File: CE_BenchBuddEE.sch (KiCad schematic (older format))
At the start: 0 parts

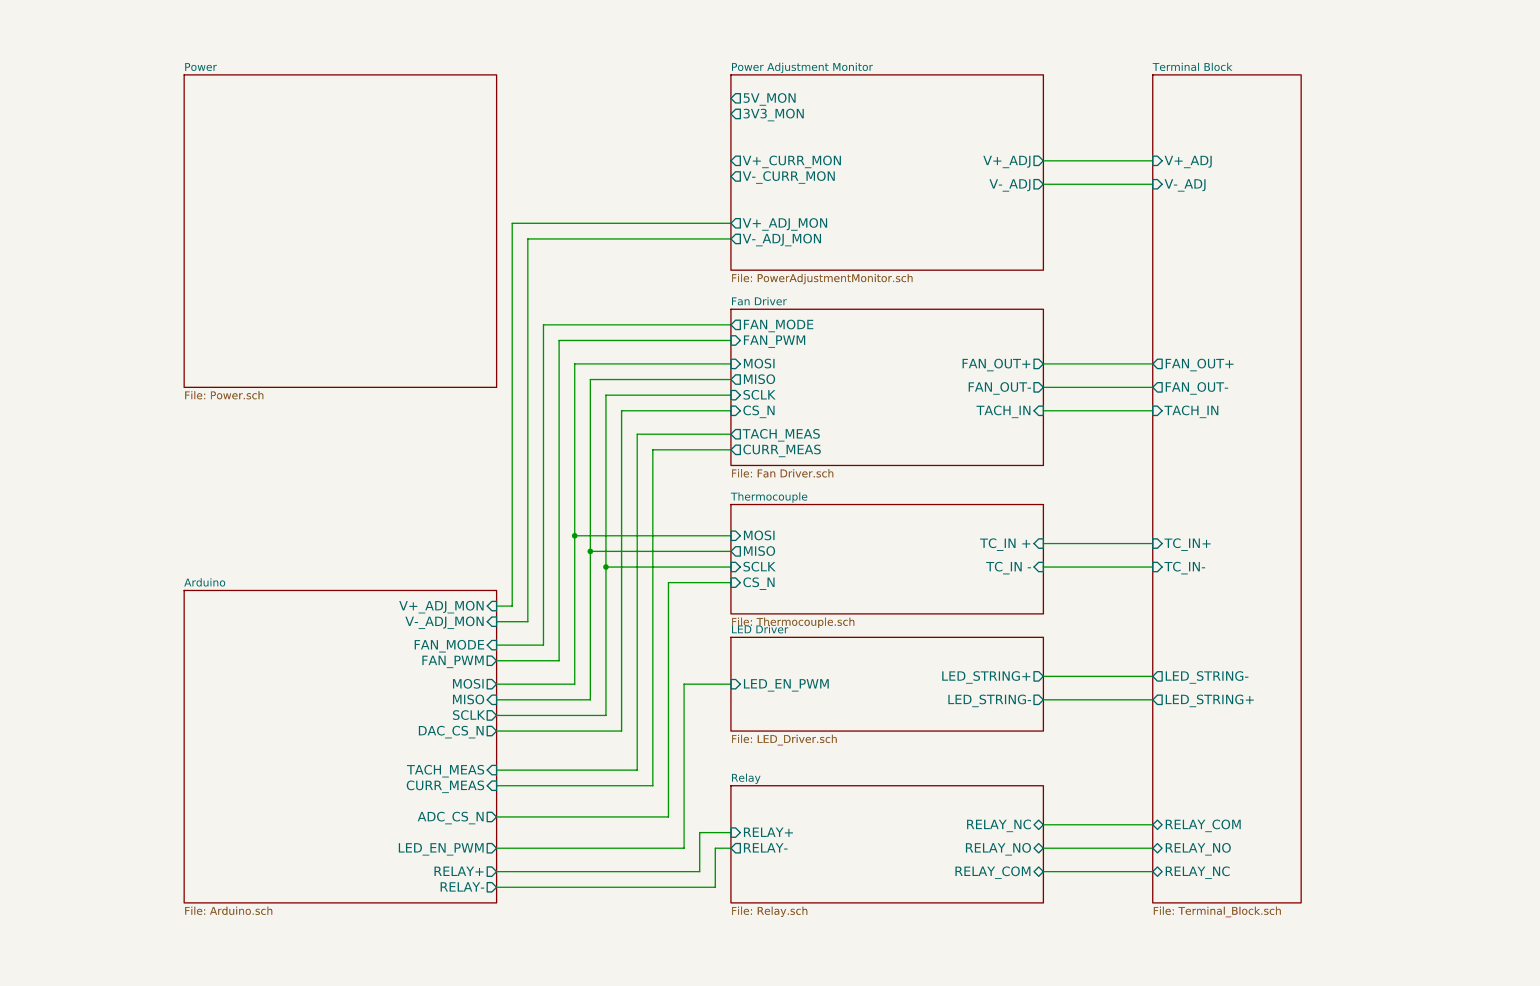
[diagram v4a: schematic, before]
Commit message: Initial layout of relay and thermocouple
All block diagrams completed through Week 3.  Component selection
spreadsheets created: Bench Buddy Session 1CE.xlsx = official part
selection and bom.xlsx is the version I came up with.

Part association and initial layout of the Relay and Thermocouple
sections completed.
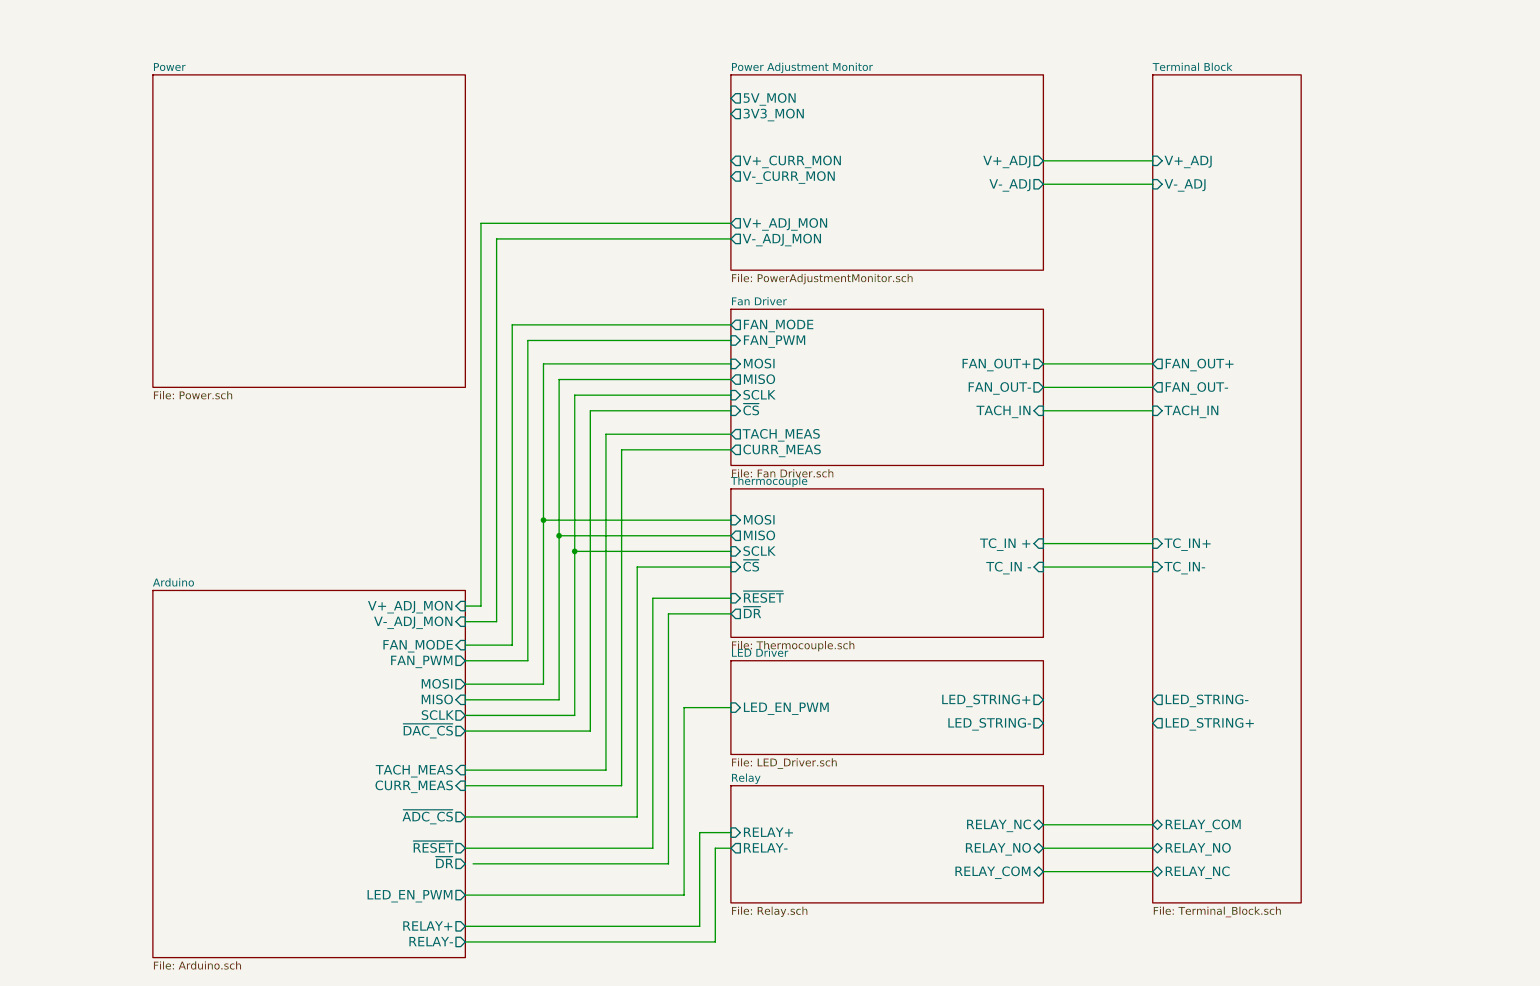
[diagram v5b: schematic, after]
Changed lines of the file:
@@
 Sheet 1 9
 Title ""
-Date "6 feb 2014"
+Date "21 feb 2014"
 Rev ""
 Comp ""
@@
 $EndDescr
 $Sheet
-S 5400 4150 2000 700
+S 5400 4050 2000 950
 U 52EBF2F6
 F0 "Thermocouple" 50
 F1 "Thermocouple.sch" 50
-F2 "MOSI" I L 5400 4350 60
-F3 "MISO" O L 5400 4450 60
-F4 "SCLK" I L 5400 4550 60
-F5 "CS_N" I L 5400 4650 60
-F6 "TC_IN +" I R 7400 4400 60
-F7 "TC_IN -" I R 7400 4550 60
+F2 "MOSI" I L 5400 4250 60
+F3 "MISO" O L 5400 4350 60
+F4 "SCLK" I L 5400 4450 60
+F5 "TC_IN +" I R 7400 4400 60
+F6 "TC_IN -" I R 7400 4550 60
+F7 "~CS" I L 5400 4550 60
+F8 "~RESET" I L 5400 4750 60
+F9 "~DR" O L 5400 4850 60
 $EndSheet
 $Sheet
@@
 $EndSheet
 $Sheet
-S 1900 1400 2000 2000
+S 1700 1400 2000 2000
 U 52EBF30F
 F0 "Power" 50
@@
 $EndSheet
 $Sheet
-S 5400 5000 2000 600
+S 5400 5150 2000 600
 U 52EBF33E
 F0 "LED Driver" 50
 F1 "LED_Driver.sch" 50
-F2 "LED_EN_PWM" I L 5400 5300 60
-F3 "LED_STRING+" O R 7400 5250 60
-F4 "LED_STRING-" O R 7400 5400 60
+F2 "LED_EN_PWM" I L 5400 5450 60
+F3 "LED_STRING+" O R 7400 5400 60
+F4 "LED_STRING-" O R 7400 5550 60
 $EndSheet
 $Sheet
@@
 F2 "MOSI" I L 5400 3250 60
 F3 "MISO" O L 5400 3350 60
-F4 "CS_N" I L 5400 3550 60
+F4 "~CS" I L 5400 3550 60
 F5 "SCLK" I L 5400 3450 60
 F6 "FAN_OUT+" O R 7400 3250 60
@@
 F5 "FAN_OUT-" O L 8100 3400 60
 F6 "TACH_IN" I L 8100 3550 60
-F7 "LED_STRING+" O L 8100 5400 60
-F8 "LED_STRING-" O L 8100 5250 60
+F7 "LED_STRING+" O L 8100 5550 60
+F8 "LED_STRING-" O L 8100 5400 60
 F9 "TC_IN+" I L 8100 4400 60
 F10 "TC_IN-" I L 8100 4550 60
@@
 F13 "RELAY_NC" B L 8100 6500 60
 $EndSheet
-$Sheet
-S 1900 4700 2000 2000
+Wire Wire Line
+	8100 1950 7400 1950
+Wire Wire Line
+	8100 2100 7400 2100
+Wire Wire Line
+	7400 3250 8100 3250
+Wire Wire Line
+	7400 3400 8100 3400
+Wire Wire Line
+	8100 3550 7400 3550
+Wire Wire Line
+	7400 4400 8100 4400
+Wire Wire Line
+	8100 4550 7400 4550
+Wire Wire Line
+	7400 6200 8100 6200
+Wire Wire Line
+	7400 6350 8100 6350
+Wire Wire Line
+	7400 6500 8100 6500
+Wire Wire Line
+	3700 4800 3800 4800
+Wire Wire Line
+	3800 4800 3800 2350
+Wire Wire Line
+	3800 2350 5400 2350
+Wire Wire Line
+	5400 2450 3900 2450
+Wire Wire Line
+	3900 2450 3900 4900
+Wire Wire Line
+	3900 4900 3700 4900
+Wire Wire Line
+	5400 3700 4600 3700
+Wire Wire Line
+	5400 3800 4700 3800
+Wire Wire Line
+	3700 5850 4600 5850
+Wire Wire Line
+	4600 5850 4600 3700
+Wire Wire Line
+	4700 3800 4700 5950
+Wire Wire Line
+	4700 5950 3700 5950
+Wire Wire Line
+	4800 6150 3700 6150
+Wire Wire Line
+	4800 4550 4800 6150
+Wire Wire Line
+	5100 5450 5100 6650
+Wire Wire Line
+	5100 5450 5400 5450
+Wire Wire Line
+	5200 6250 5200 6850
+Wire Wire Line
+	5200 6250 5400 6250
+Wire Wire Line
+	5400 6350 5300 6350
+Wire Wire Line
+	5300 6350 5300 6950
+Wire Wire Line
+	4200 5300 3700 5300
+Wire Wire Line
+	4300 5400 3700 5400
+Wire Wire Line
+	4400 5500 3700 5500
+Wire Wire Line
+	3700 5600 4500 5600
+Wire Wire Line
+	5400 3100 4100 3100
+Wire Wire Line
+	4100 3100 4100 5150
+Wire Wire Line
+	4100 5150 3700 5150
+Wire Wire Line
+	3700 5050 4000 5050
+Wire Wire Line
+	4000 5050 4000 3000
+Wire Wire Line
+	4000 3000 5400 3000
+Wire Wire Line
+	4500 3550 5400 3550
+Wire Wire Line
+	4400 3450 5400 3450
+Wire Wire Line
+	4300 3350 5400 3350
+Wire Wire Line
+	4200 3250 5400 3250
+Wire Wire Line
+	4200 3250 4200 5300
+Wire Wire Line
+	4300 3350 4300 5400
+Wire Wire Line
+	4400 3450 4400 5500
+Wire Wire Line
+	4500 5600 4500 3550
+$Sheet
+S 1700 4700 2000 2350
 U 52EBF29E
 F0 "Arduino" 50
 F1 "Arduino.sch" 50
-F2 "MOSI" O R 3900 5300 60
-F3 "MISO" I R 3900 5400 60
-F4 "SCLK" O R 3900 5500 60
-F5 "TACH_MEAS" I R 3900 5850 60
-F6 "LED_EN_PWM" O R 3900 6350 60
-F7 "CURR_MEAS" I R 3900 5950 60
-F8 "RELAY+" O R 3900 6500 60
-F9 "RELAY-" O R 3900 6600 60
-F10 "V+_ADJ_MON" I R 3900 4800 60
-F11 "V-_ADJ_MON" I R 3900 4900 60
-F12 "DAC_CS_N" O R 3900 5600 60
-F13 "ADC_CS_N" O R 3900 6150 60
-F14 "FAN_PWM" O R 3900 5150 60
-F15 "FAN_MODE" I R 3900 5050 60
-$EndSheet
-Wire Wire Line
-	8100 1950 7400 1950
-Wire Wire Line
-	8100 2100 7400 2100
-Wire Wire Line
-	7400 3250 8100 3250
-Wire Wire Line
-	7400 3400 8100 3400
-Wire Wire Line
-	8100 3550 7400 3550
-Wire Wire Line
-	7400 4400 8100 4400
-Wire Wire Line
-	8100 4550 7400 4550
-Wire Wire Line
-	7400 5250 8100 5250
-Wire Wire Line
-	7400 5400 8100 5400
-Wire Wire Line
-	7400 6200 8100 6200
-Wire Wire Line
-	7400 6350 8100 6350
-Wire Wire Line
-	7400 6500 8100 6500
-Wire Wire Line
-	3900 4800 4000 4800
-Wire Wire Line
-	4000 4800 4000 2350
-Wire Wire Line
-	4000 2350 5400 2350
-Wire Wire Line
-	5400 2450 4100 2450
-Wire Wire Line
-	4100 2450 4100 4900
-Wire Wire Line
-	4100 4900 3900 4900
-Wire Wire Line
-	5400 3700 4800 3700
-Wire Wire Line
-	5400 3800 4900 3800
-Wire Wire Line
-	3900 5850 4800 5850
-Wire Wire Line
-	4800 5850 4800 3700
-Wire Wire Line
-	4900 3800 4900 5950
-Wire Wire Line
-	4900 5950 3900 5950
-Wire Wire Line
-	3900 6150 5000 6150
-Wire Wire Line
-	5000 6150 5000 4650
-Wire Wire Line
-	5000 4650 5400 4650
-Wire Wire Line
-	3900 6350 5100 6350
-Wire Wire Line
-	5100 6350 5100 5300
-Wire Wire Line
-	5100 5300 5400 5300
-Wire Wire Line
-	3900 6500 5200 6500
-Wire Wire Line
-	5200 6500 5200 6250
-Wire Wire Line
-	5200 6250 5400 6250
-Wire Wire Line
-	5400 6350 5300 6350
-Wire Wire Line
-	5300 6350 5300 6600
-Wire Wire Line
-	5300 6600 3900 6600
-Wire Wire Line
-	4400 5300 3900 5300
-Wire Wire Line
-	4500 5400 3900 5400
-Wire Wire Line
-	4600 5500 3900 5500
-Wire Wire Line
-	5400 4350 4400 4350
-Connection ~ 4400 4350
-Wire Wire Line
-	5400 4450 4500 4450
-Connection ~ 4500 4450
-Wire Wire Line
-	5400 4550 4600 4550
-Connection ~ 4600 4550
-Wire Wire Line
-	3900 5600 4700 5600
-Wire Wire Line
-	5400 3100 4300 3100
-Wire Wire Line
-	4300 3100 4300 5150
-Wire Wire Line
-	4300 5150 3900 5150
-Wire Wire Line
-	3900 5050 4200 5050
-Wire Wire Line
-	4200 5050 4200 3000
-Wire Wire Line
-	4200 3000 5400 3000
-Wire Wire Line
-	4700 3550 5400 3550
-Wire Wire Line
-	4600 3450 5400 3450
-Wire Wire Line
-	4500 3350 5400 3350
-Wire Wire Line
-	4400 3250 5400 3250
-Wire Wire Line
-	4400 3250 4400 5300
-Wire Wire Line
-	4500 3350 4500 5400
-Wire Wire Line
-	4600 3450 4600 5500
-Wire Wire Line
-	4700 5600 4700 3550
+F2 "MOSI" O R 3700 5300 60
+F3 "MISO" I R 3700 5400 60
+F4 "SCLK" O R 3700 5500 60
+F5 "TACH_MEAS" I R 3700 5850 60
+F6 "LED_EN_PWM" O R 3700 6650 60
+F7 "CURR_MEAS" I R 3700 5950 60
+F8 "RELAY+" O R 3700 6850 60
+F9 "RELAY-" O R 3700 6950 60
+F10 "V+_ADJ_MON" I R 3700 4800 60
+F11 "V-_ADJ_MON" I R 3700 4900 60
+F12 "FAN_PWM" O R 3700 5150 60
+F13 "FAN_MODE" I R 3700 5050 60
+F14 "~RESET" O R 3700 6350 60
+F15 "~DR" O R 3700 6450 60
+F16 "~DAC_CS" O R 3700 5600 60
+F17 "~ADC_CS" O R 3700 6150 60
+$EndSheet
+Wire Wire Line
+	5400 4250 4200 4250
+Connection ~ 4200 4250
+Wire Wire Line
+	5400 4350 4300 4350
+Connection ~ 4300 4350
+Wire Wire Line
+	5400 4450 4400 4450
+Connection ~ 4400 4450
+Wire Wire Line
+	4800 4550 5400 4550
+Wire Wire Line
+	5400 4750 4900 4750
+Wire Wire Line
+	4900 4750 4900 6350
+Wire Wire Line
+	4900 6350 3700 6350
+Wire Wire Line
+	3750 6450 5000 6450
+Wire Wire Line
+	5000 6450 5000 4850
+Wire Wire Line
+	5000 4850 5400 4850
+Wire Wire Line
+	5100 6650 3700 6650
+Wire Wire Line
+	5200 6850 3700 6850
+Wire Wire Line
+	5300 6950 3700 6950
 $EndSCHEMATC

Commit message: Initial layout of Arduino and Fan-Current
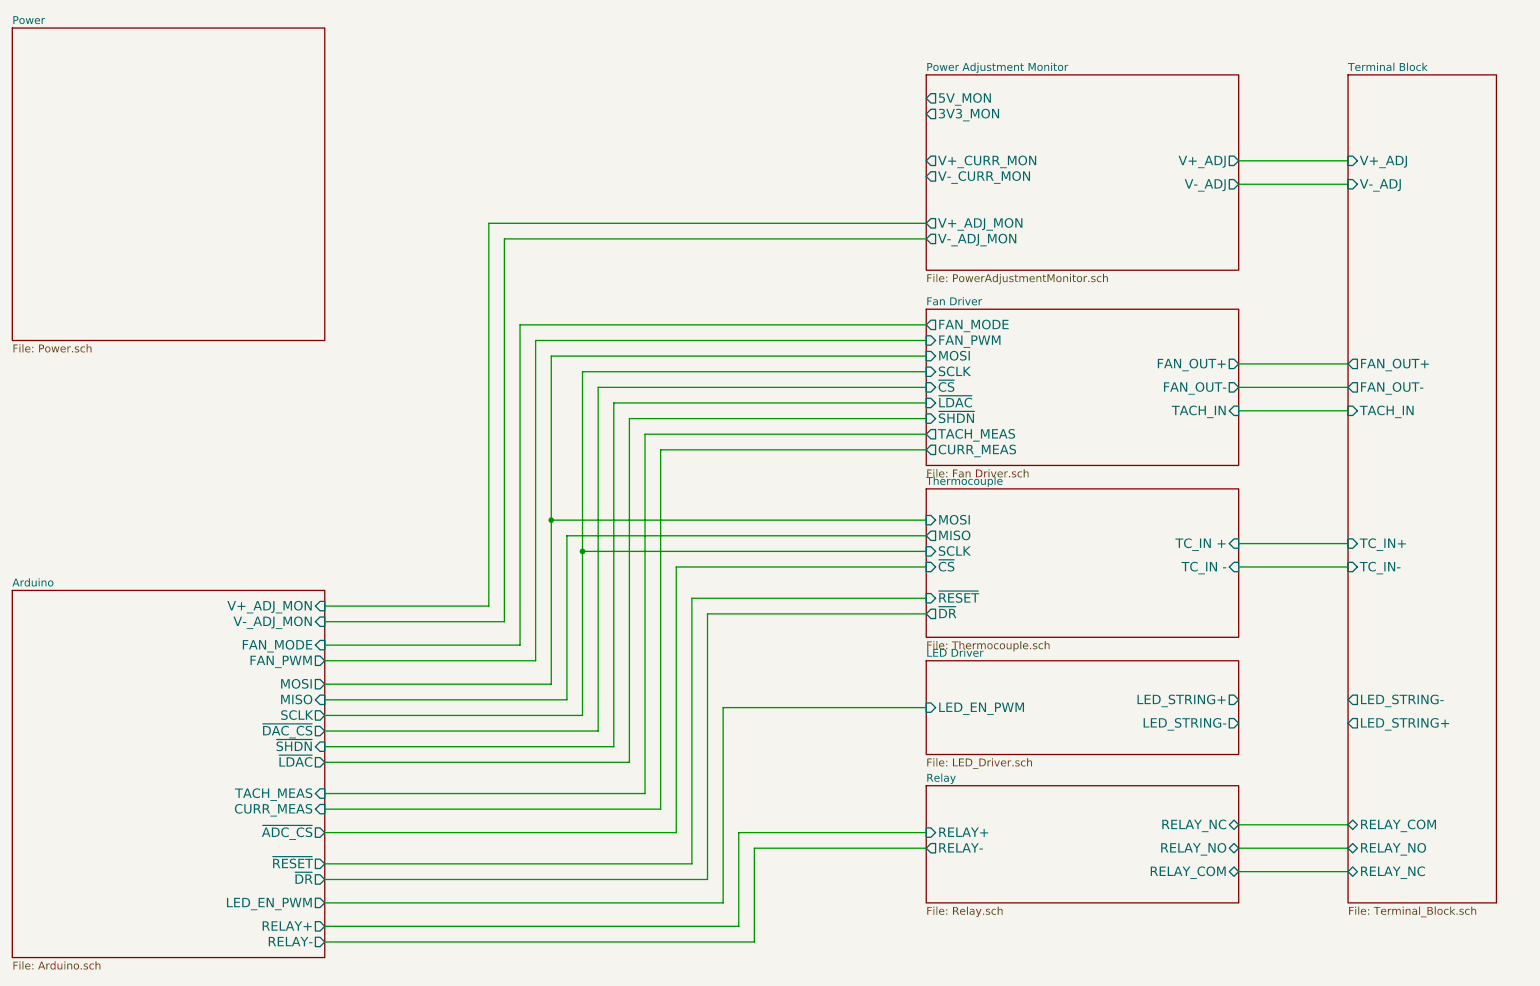
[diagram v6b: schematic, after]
